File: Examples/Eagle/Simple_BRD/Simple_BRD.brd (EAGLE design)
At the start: 15.2 x 33 mm, 2 parts

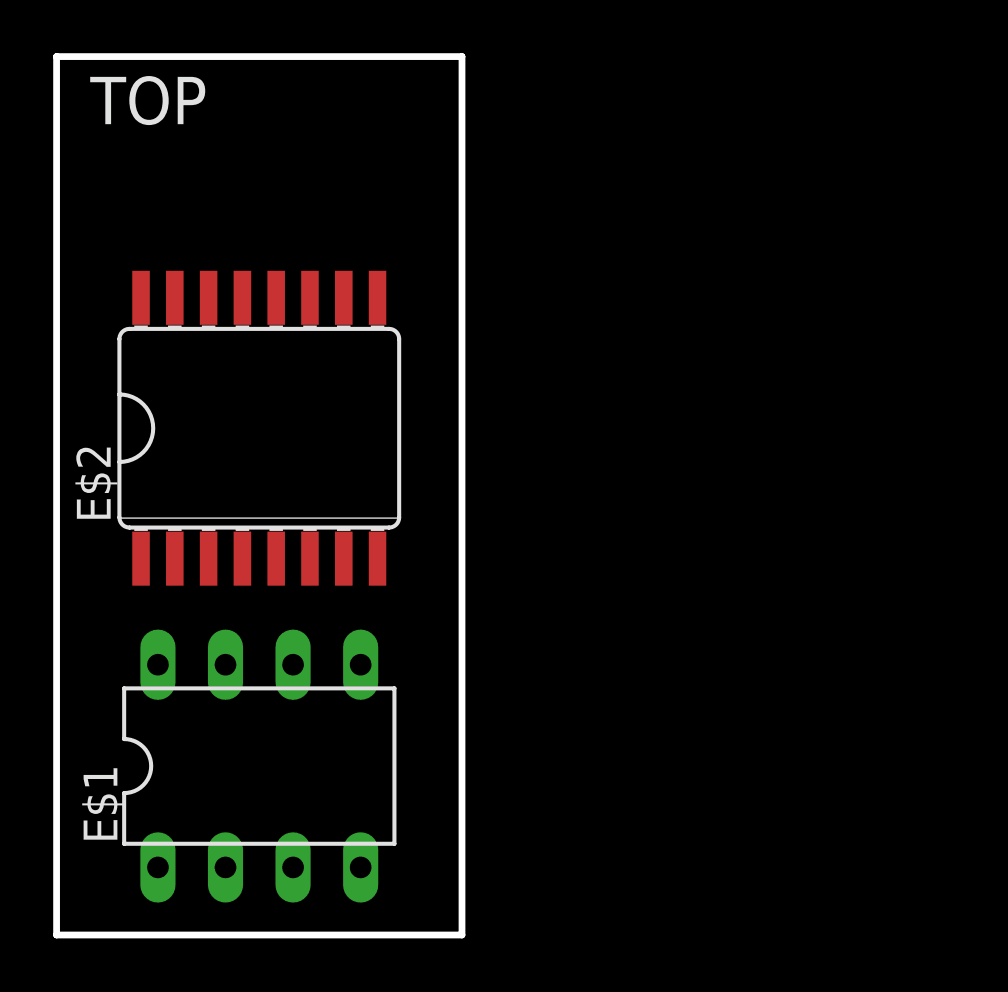
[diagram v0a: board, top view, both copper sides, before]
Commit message: Updated simple board to have curved edges
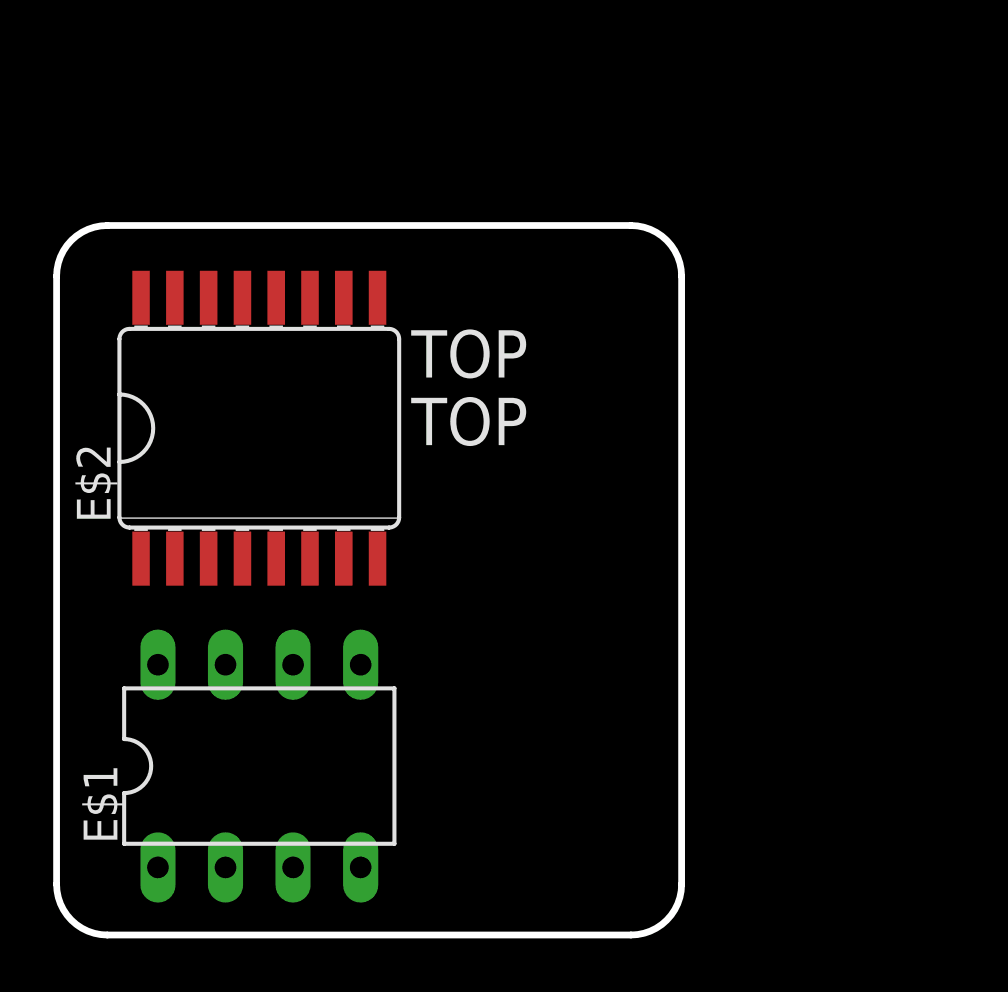
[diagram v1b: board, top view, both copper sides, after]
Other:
- board size 15.2 x 33 mm -> 23.5 x 26.7 mm
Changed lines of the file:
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@@
 <setting verticaltext="up"/>
 </settings>
-<grid distance="0.05" unitdist="inch" unit="inch" style="lines" multiple="1" display="yes" altdistance="0.005" altunitdist="inch" altunit="inch"/>
+<grid distance="0.025" unitdist="inch" unit="inch" style="lines" multiple="1" display="yes" altdistance="0.005" altunitdist="inch" altunit="inch"/>
 <layers>
 <layer number="1" name="Top" color="4" fill="1" visible="yes" active="yes"/>
@@
 <board>
 <plain>
-<wire x1="0" y1="0" x2="0" y2="33.02" width="0.254" layer="20"/>
-<wire x1="0" y1="33.02" x2="15.24" y2="33.02" width="0.254" layer="20"/>
-<wire x1="15.24" y1="33.02" x2="15.24" y2="0" width="0.254" layer="20"/>
-<wire x1="15.24" y1="0" x2="0" y2="0" width="0.254" layer="20"/>
-<text x="1.27" y="30.48" size="1.778" layer="21" font="vector" ratio="15">TOP</text>
-<text x="10.16" y="30.48" size="1.778" layer="27" font="vector" ratio="15">TOP</text>
-<text x="1.27" y="29.21" size="1.778" layer="28" font="vector" ratio="15" rot="R270">BOTTOM</text>
-<text x="12.7" y="29.21" size="1.778" layer="27" font="vector" ratio="15" rot="R270">BOTTOM</text>
+<wire x1="0" y1="1.905" x2="0" y2="24.765" width="0.254" layer="20"/>
+<wire x1="1.905" y1="26.67" x2="21.59" y2="26.67" width="0.254" layer="20"/>
+<wire x1="23.495" y1="24.765" x2="23.495" y2="1.905" width="0.254" layer="20"/>
+<wire x1="21.59" y1="0" x2="1.905" y2="0" width="0.254" layer="20"/>
+<text x="13.335" y="18.415" size="1.778" layer="25" font="vector" ratio="15">TOP</text>
+<text x="13.335" y="15.875" size="1.778" layer="27" font="vector" ratio="15">TOP</text>
+<text x="13.335" y="6.35" size="1.778" layer="26" font="vector" ratio="15">BOTTOM</text>
+<text x="13.335" y="3.81" size="1.778" layer="28" font="vector" ratio="15">BOTTOM</text>
+<wire x1="0" y1="24.765" x2="1.905" y2="26.67" width="0.254" layer="20" curve="-90"/>
+<wire x1="21.59" y1="26.67" x2="23.495" y2="24.765" width="0.254" layer="20" curve="-90"/>
+<wire x1="1.905" y1="0" x2="0" y2="1.905" width="0.254" layer="20" curve="-90"/>
+<wire x1="23.495" y1="1.905" x2="21.59" y2="0" width="0.254" layer="20" curve="-90"/>
+<text x="13.335" y="8.89" size="1.778" layer="22" font="vector" ratio="15">BOTTOM</text>
+<text x="13.335" y="20.955" size="1.778" layer="21" font="vector" ratio="15">TOP</text>
 </plain>
 <attributes>

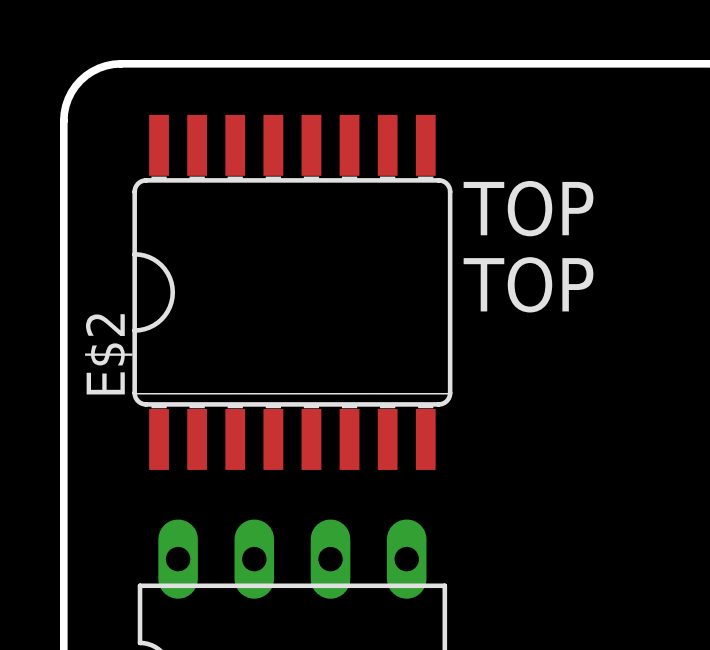
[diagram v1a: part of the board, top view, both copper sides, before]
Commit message: Stared updating Eagle ULP and render.js for new data interchange format
Data interchange format for PCB shape and header information has been
completed.
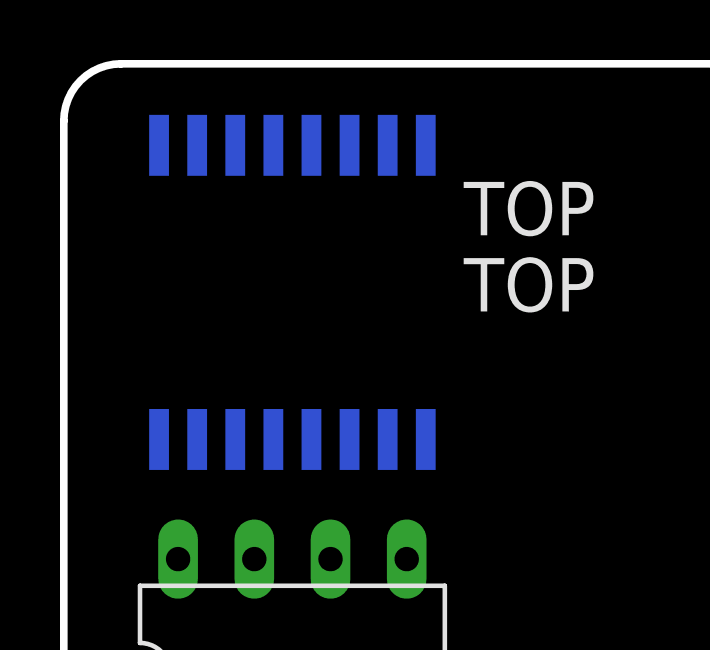
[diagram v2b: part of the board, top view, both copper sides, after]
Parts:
- flipped E$2 to the bottom, turned to 180 degrees
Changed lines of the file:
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@@
 <setting verticaltext="up"/>
 </settings>
-<grid distance="0.025" unitdist="inch" unit="inch" style="lines" multiple="1" display="yes" altdistance="0.005" altunitdist="inch" altunit="inch"/>
+<grid distance="0.05" unitdist="inch" unit="inch" style="lines" multiple="1" display="yes" altdistance="0.005" altunitdist="inch" altunit="inch"/>
 <layers>
 <layer number="1" name="Top" color="4" fill="1" visible="yes" active="yes"/>
@@
 <attribute name="VALUE" x="4.064" y="5.715" size="1.27" layer="27" ratio="10"/>
 </element>
-<element name="E$2" library="74xx-us" library_urn="urn:adsk.eagle:library:88" package="SO16L" package3d_urn="urn:adsk.eagle:package:17518/1" value="" x="7.62" y="19.05" smashed="yes">
-<attribute name="NAME" x="2.032" y="15.494" size="1.27" layer="25" ratio="10" rot="R90"/>
-<attribute name="VALUE" x="4.064" y="18.288" size="1.27" layer="27" ratio="10"/>
+<element name="E$2" library="74xx-us" library_urn="urn:adsk.eagle:library:88" package="SO16L" package3d_urn="urn:adsk.eagle:package:17518/1" value="" x="7.62" y="19.05" smashed="yes" rot="MR180">
+<attribute name="NAME" x="2.032" y="22.606" size="1.27" layer="26" ratio="10" rot="MR270"/>
+<attribute name="VALUE" x="4.064" y="19.812" size="1.27" layer="28" ratio="10" rot="MR180"/>
 </element>
 </elements>

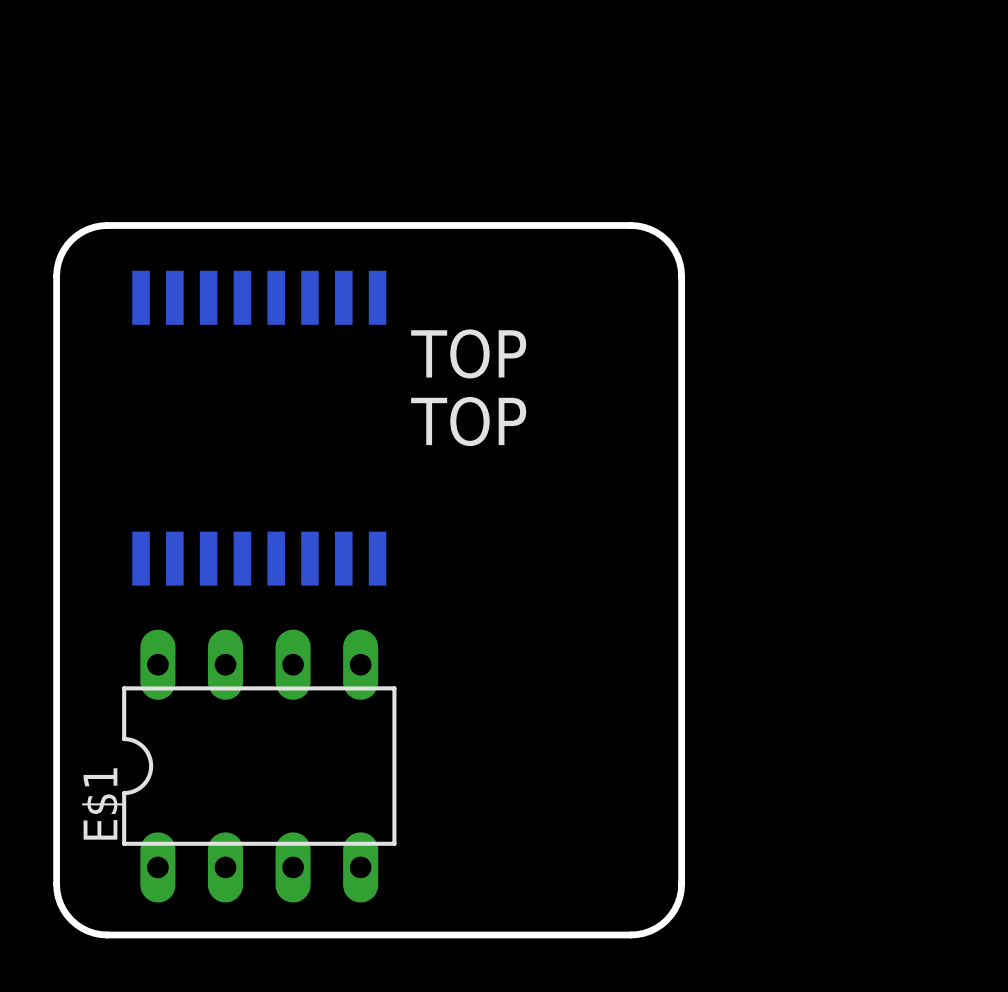
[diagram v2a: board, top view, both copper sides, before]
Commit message: Updated example board to be more complex
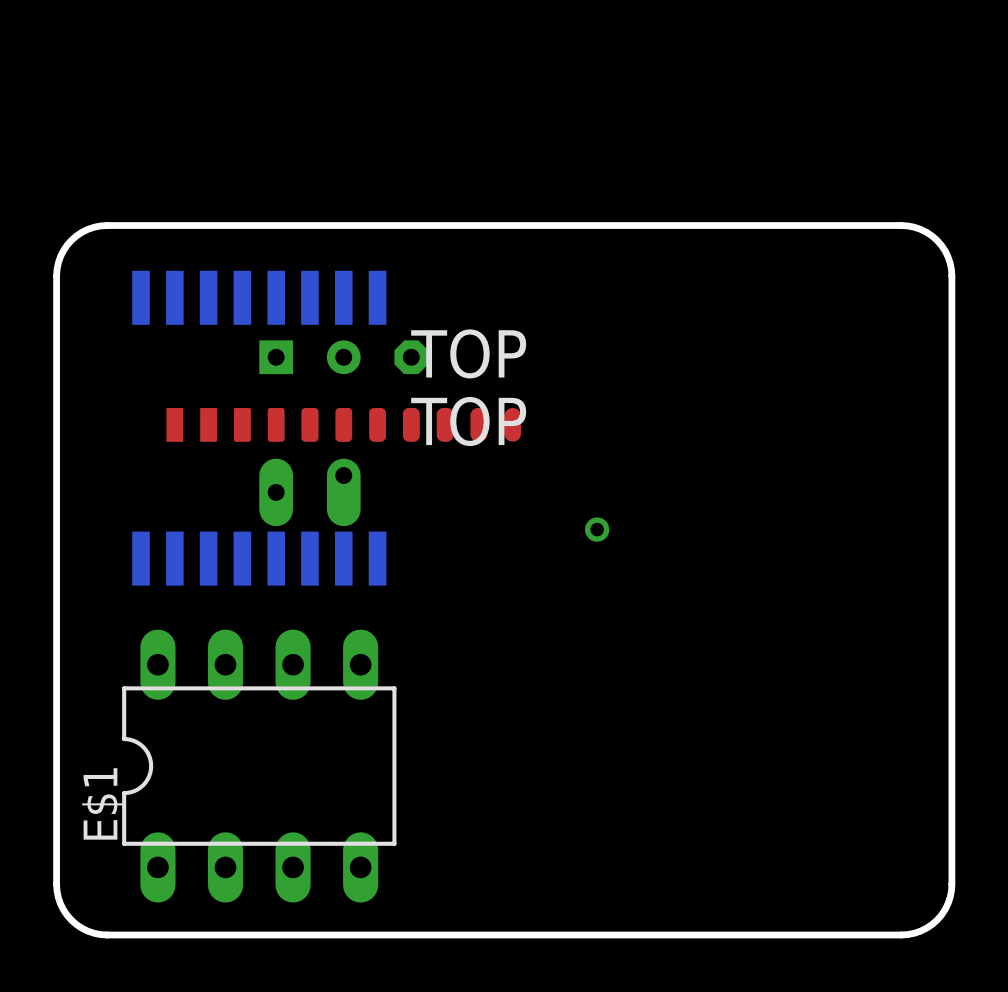
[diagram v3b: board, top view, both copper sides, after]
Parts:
- added E$3: (no value), untitled:TEST
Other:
- board size 23.5 x 26.7 mm -> 33.7 x 26.7 mm
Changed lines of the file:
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@@
 <setting verticaltext="up"/>
 </settings>
-<grid distance="0.05" unitdist="inch" unit="inch" style="lines" multiple="1" display="yes" altdistance="0.005" altunitdist="inch" altunit="inch"/>
+<grid distance="0.05" unitdist="inch" unit="mil" style="lines" multiple="1" display="yes" altdistance="25" altunitdist="mil" altunit="mil"/>
 <layers>
 <layer number="1" name="Top" color="4" fill="1" visible="yes" active="yes"/>
@@
 <layer number="51" name="tDocu" color="7" fill="1" visible="yes" active="yes"/>
 <layer number="52" name="bDocu" color="7" fill="1" visible="yes" active="yes"/>
+<layer number="88" name="SimResults" color="9" fill="1" visible="no" active="no"/>
+<layer number="89" name="SimProbes" color="9" fill="1" visible="no" active="no"/>
+<layer number="90" name="Modules" color="5" fill="1" visible="no" active="no"/>
 <layer number="91" name="Nets" color="2" fill="1" visible="no" active="no"/>
 <layer number="92" name="Busses" color="1" fill="1" visible="no" active="no"/>
@@
 <plain>
 <wire x1="0" y1="1.905" x2="0" y2="24.765" width="0.254" layer="20"/>
-<wire x1="1.905" y1="26.67" x2="21.59" y2="26.67" width="0.254" layer="20"/>
-<wire x1="23.495" y1="24.765" x2="23.495" y2="1.905" width="0.254" layer="20"/>
-<wire x1="21.59" y1="0" x2="1.905" y2="0" width="0.254" layer="20"/>
+<wire x1="1.905" y1="26.67" x2="31.75" y2="26.67" width="0.254" layer="20"/>
+<wire x1="33.655" y1="24.765" x2="33.655" y2="1.905" width="0.254" layer="20"/>
+<wire x1="31.75" y1="0" x2="1.905" y2="0" width="0.254" layer="20"/>
 <text x="13.335" y="18.415" size="1.778" layer="25" font="vector" ratio="15">TOP</text>
 <text x="13.335" y="15.875" size="1.778" layer="27" font="vector" ratio="15">TOP</text>
@@
 <text x="13.335" y="3.81" size="1.778" layer="28" font="vector" ratio="15">BOTTOM</text>
 <wire x1="0" y1="24.765" x2="1.905" y2="26.67" width="0.254" layer="20" curve="-90"/>
-<wire x1="21.59" y1="26.67" x2="23.495" y2="24.765" width="0.254" layer="20" curve="-90"/>
+<wire x1="31.75" y1="26.67" x2="33.655" y2="24.765" width="0.254" layer="20" curve="-90"/>
 <wire x1="1.905" y1="0" x2="0" y2="1.905" width="0.254" layer="20" curve="-90"/>
-<wire x1="23.495" y1="1.905" x2="21.59" y2="0" width="0.254" layer="20" curve="-90"/>
+<wire x1="33.655" y1="1.905" x2="31.75" y2="0" width="0.254" layer="20" curve="-90"/>
 <text x="13.335" y="8.89" size="1.778" layer="22" font="vector" ratio="15">BOTTOM</text>
 <text x="13.335" y="20.955" size="1.778" layer="21" font="vector" ratio="15">TOP</text>
@@
 <attribute name="VALUE" x="4.064" y="19.812" size="1.27" layer="28" ratio="10" rot="MR180"/>
 </element>
+<element name="E$3" library="untitled" package="TEST" value="" x="8.255" y="21.717" smashed="yes"/>
 </elements>
 <signals>
+<signal name="S$1">
+<via x="20.32" y="15.24" extent="1-16" drill="0.508"/>
+</signal>
 </signals>
 <mfgpreviewcolors>
